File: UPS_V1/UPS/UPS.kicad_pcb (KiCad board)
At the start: 2 copper layers, 48.7 x 54.1 mm, 84 parts, among them J1 Conn_01x02_Pin, J2 Conn_01x02_Pin, J3 USB_B_Micro, J4 Conn_01x02_Socket, J5 Conn_01x02_Pin, J6 Conn_01x02_Socket, J7 Conn_01x02_Pin, J8 Screw_Terminal_01x02, J9 Screw_Terminal_01x02, U1 MT3608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

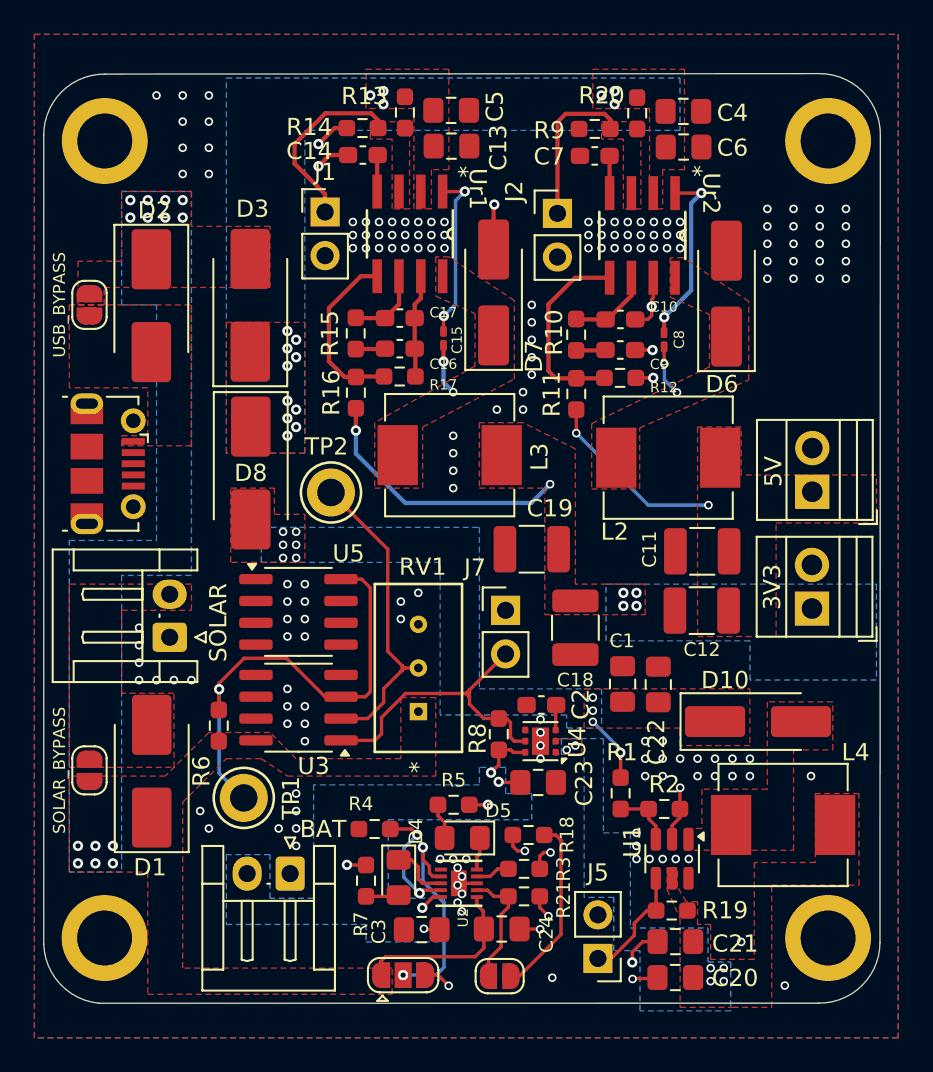
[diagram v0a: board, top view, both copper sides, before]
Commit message: added 1x12 terminal block
 1x12 terminal block
3d
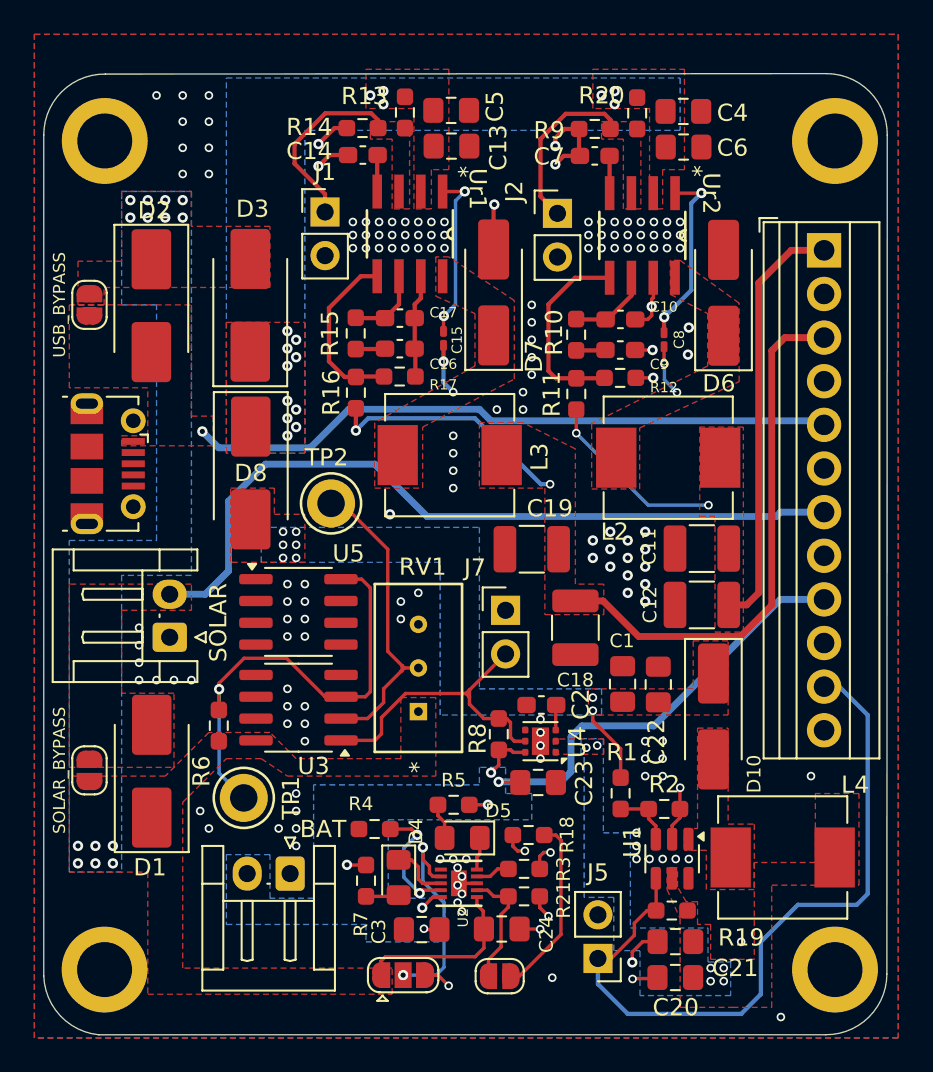
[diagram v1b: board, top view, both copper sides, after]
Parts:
- removed J9: Screw_Terminal_01x02, TerminalBlock:TerminalBlock_Xinya_XY308-2.54-2P_1x02_P2.54mm_Horizontal
- J8: value Screw_Terminal_01x02 -> PROVISIONAL_PORTS; footprint TerminalBlock:TerminalBlock_Xinya_XY308-2.54-2P_1x02_P2.54mm_Horizontal -> TerminalBlock:TerminalBlock_Xinya_XY308-2.54-12P_1x12_P2.54mm_Horizontal
- moved J8 20.9 mm to (159.8, 44.6), turned to -90 degrees
- moved D10 2.62 mm to (153.3, 71.7), turned to -90 degrees
- moved L4 1.89 mm to (157.4, 79.9)
- moved H2 1.88 mm to (160.4, 86.4)
- moved H1 1.84 mm to (117.9, 86.4)
- moved TP2 0.64 mm to (131.1, 59.3)
- moved H3 0.40 mm to (160.4, 38.2)
- moved C12 0.33 mm to (152.7, 65.2)
- moved D6 0.18 mm to (153.9, 47.0)
- moved C11 0.16 mm to (152.7, 61.9)
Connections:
- J5 pad 1: Net-(J5-Pin_1) -> BOOST_EN
- J8 pad 1: 3.3VOUT -> 5VOUT
- R19 pad 2: Net-(J5-Pin_1) -> BOOST_EN
- U1 pad 4: Net-(J5-Pin_1) -> BOOST_EN
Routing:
- net SOLAR IN: track 0.00 -> 45.0 mm
- net BOOST_EN: track 0.00 -> 43.1 mm
- net DC IN: track 0.00 -> 37.9 mm, vias 0 -> 1
- net 3.3VOUT: track 15.6 -> 45.7 mm, vias 6 -> 2
- net 5VOUT: track 10.8 -> 35.5 mm
- net BATT +: track 8.86 -> 33.4 mm
- net Net-(J5-Pin_1): track 6.84 -> 0.00 mm
- net GND: track 33.1 -> 38.4 mm, vias 173 -> 163
- net Net-(J2-Pin_1): track 9.27 -> 10.1 mm
- net Net-(D10-K): track 3.92 -> 4.57 mm, vias 10 -> 8
- removed copper zone on B.Cu, net 3.3VOUT
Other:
- board size 48.7 x 54.1 mm -> 49.1 x 56 mm
- board text added: "BATTERY"
- board text added: "BOOST_EN"
- board text added: "CTRL"
- board text added: "DC_IN"
- board text added: "DESIGN NOTES: VIAS SIZE: 0.6 & 0.3 0.5 & 0.3 TRACK SIZE USED: 0.4 0.2 0.25 COPPER ZONE FOR POWER: SOLID WITH 0.5 & 0.2 CLEARANCE COPPER ZONE FOR GND: THERMAL RELIEF 0.5 & 0.4 CLEARANCE *ADJUSTED CLEARANCE OF OTHER FOOTPRINT TOO BIG THAT CAUSES ERROR*"
- board text added: "GND"
- board text added: "INPUT"
- board text added: "OUTPUT"
- board text added: "SOLAR_IN"
- board text removed: "DESIGN NOTES: VIAS SIZE: 0.6 & 0.3 0.5 & 0.3 TRACK SIZE USED: 0.2 0.25 COPPER ZONE FOR POWER: SOLID WITH 0.5 & 0.2 CLEARANCE COPPER ZONE FOR GND: THERMAL RELIEF 0.5 & 0.4 CLEARANCE *ADJUSTED CLEARANCE OF OTHER FOOTPRINT TOO BIG THAT CAUSES ERROR*"

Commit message: minor edits
thermal reliefs
front silk designations
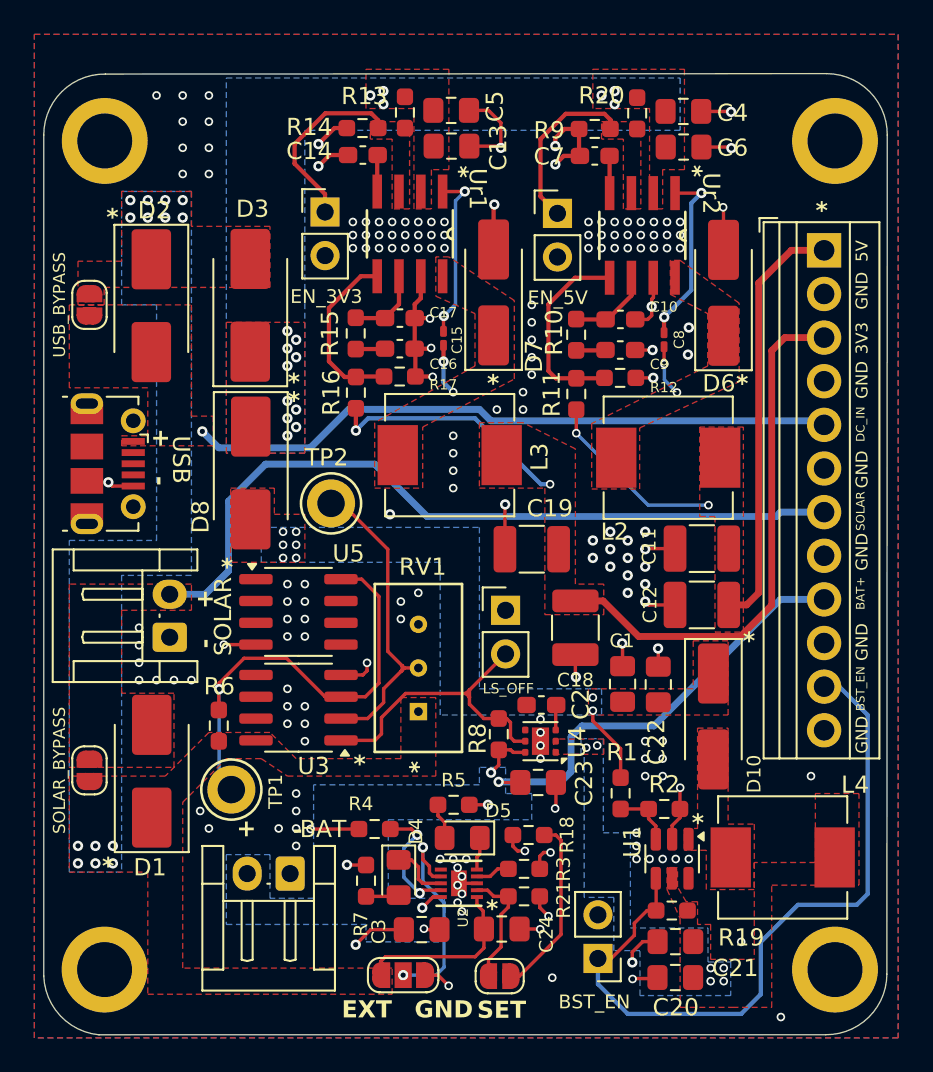
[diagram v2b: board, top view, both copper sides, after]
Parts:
- moved TP1 0.87 mm to (125.3, 76.0)
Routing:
- net GND: track 38.4 -> 75.7 mm, vias 163 -> 180
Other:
- board text added: "*"
- board text added: "BAT+"
- board text added: "BST_EN"
- board text added: "EXT"
- board text added: "SET"
- board text added: "SOLAR"

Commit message: -
edited zoning
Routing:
- net GND: vias 180 -> 259

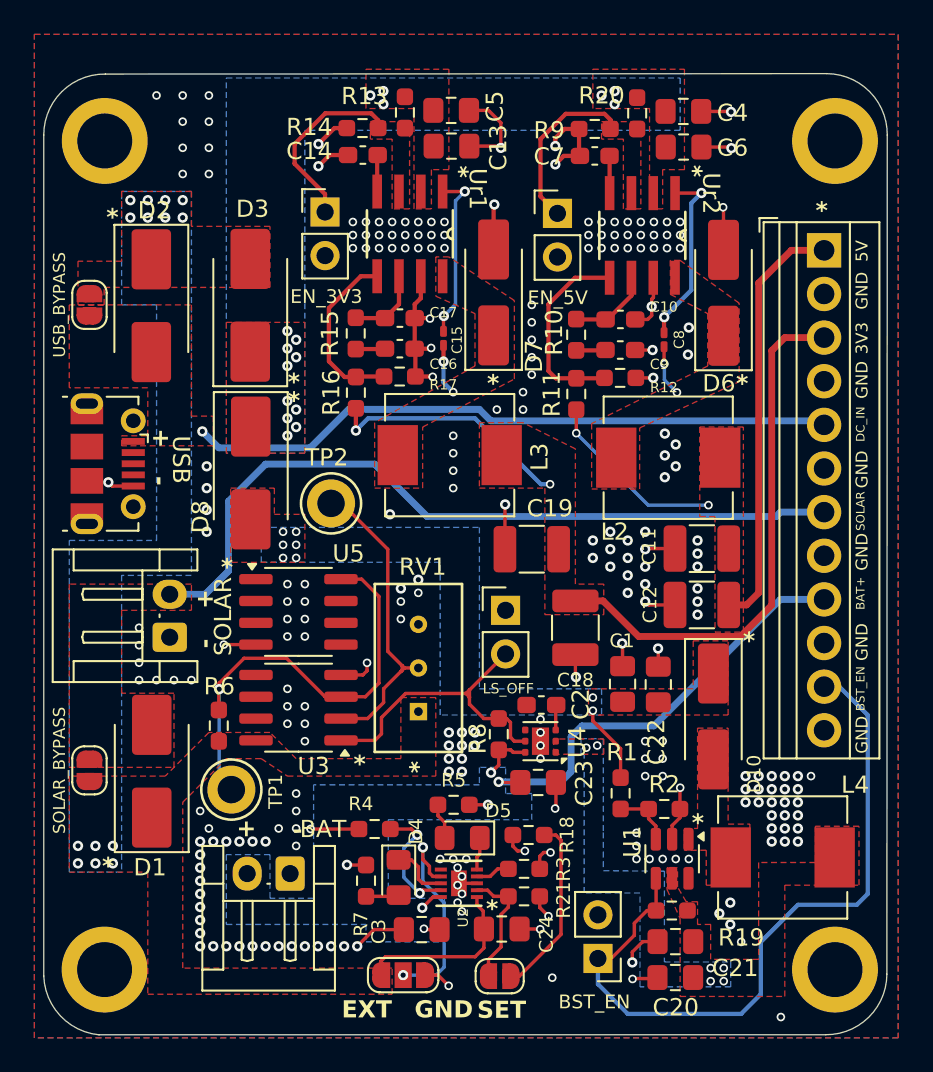
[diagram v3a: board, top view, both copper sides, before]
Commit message: Adjusted Silk Screen Front and Back
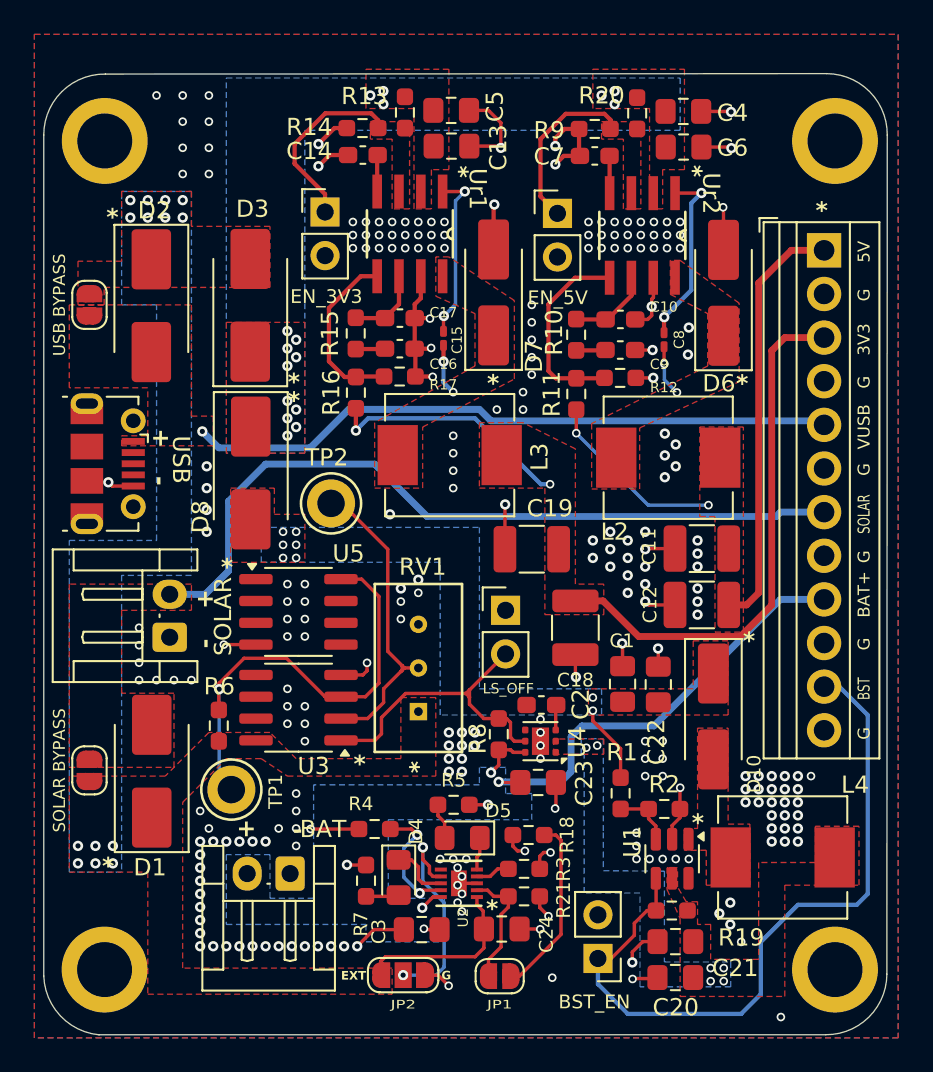
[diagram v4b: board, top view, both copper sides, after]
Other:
- board text added: "BST"
- board text added: "Charles Kim Kabiling Aernest Rivera"
- board text added: "Designed By:"
- board text added: "G"
- board text added: "INPUTS"
- board text added: "OUTPUTS"
- board text added: "VUSB"
- board text removed: "BST_EN"
- board text removed: "INPUT"
- board text removed: "OUTPUT"
- board text removed: "SET"
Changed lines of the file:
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@@
 			)
 		)
+		(model "${KICAD8_3DMODEL_DIR}/Potentiometer_THT.3dshapes/Potentiometer_Bourns_3266Y_Vertical.step"
+			(hide yes)
+			(offset
+				(xyz 5 0 0)
+			)
+			(scale
+				(xyz 1 1 1)
+			)
+			(rotate
+				(xyz 0 0 0)
+			)
+		)
+		(model "${KICAD8_3DMODEL_DIR}/Potentiometer_THT.3dshapes/Potentiometer_Bourns_3296W_Vertical.step"
+			(offset
+				(xyz 5 0 0)
+			)
+			(scale
+				(xyz 1 1 1)
+			)
+			(rotate
+				(xyz 0 0 0)
+			)
+		)
 	)
 	(footprint "Capacitor_SMD:C_0603_1608Metric_Pad1.08x0.95mm_HandSolder"
@@
 			(pintype "power_in")
 		)
-		(model "C:/Users/Aerest/Documents/GitHub/esp32PLC/UPS_V1/3D file/BQ24040DSQR/DSQ0010A.stp"
+		(model "C:/Users/ckabiling/OneDrive - Duke Manufacturing/Documents/Github/UPS/UPS_V1/3D file/BQ24040DSQR/DSQ0010A.stp"
 			(offset
 				(xyz 0 0 0)
@@
 			(pintype "power_in")
 		)
-		(model "C:/Users/Aerest/Documents/GitHub/esp32PLC/UPS_V1/3D file/TPS54331DR/D0008A.stp"
+		(model "C:/Users/ckabiling/OneDrive - Duke Manufacturing/Documents/Github/UPS/UPS_V1/3D file/TPS54331DR/D0008A.stp"
 			(offset
 				(xyz 0 0 0)
@@
 			)
 		)
-		(property "Designation" "USB_BYPASS"
+		(property "Designation" "USB BYPASS"
 			(at 0 1.75 90)
 			(unlocked yes)
@@
 		)
 		(model "C:/Users/Aerest/Documents/GitHub/esp32PLC/UPS_V1/3D file/1_282834_2/c-1-282834-2-c-3d.stp"
+			(hide yes)
 			(offset
 				(xyz 14 3.25 3)
@@
 			)
 			(rotate
-				(xyz -90 0 -180)
+				(xyz 0 0 -180)
+			)
+		)
+		(model "${KICAD8_3DMODEL_DIR}/TerminalBlock_Phoenix.3dshapes/TerminalBlock_Phoenix_MPT-0,5-6-2.54_1x06_P2.54mm_Horizontal.step"
+			(offset
+				(xyz 12.5 0 0)
+			)
+			(scale
+				(xyz 1 1 1)
+			)
+			(rotate
+				(xyz 0 0 180)
+			)
+		)
+		(model "${KICAD8_3DMODEL_DIR}/TerminalBlock_Phoenix.3dshapes/TerminalBlock_Phoenix_MPT-0,5-6-2.54_1x06_P2.54mm_Horizontal.step"
+			(offset
+				(xyz 28 0 0)
+			)
+			(scale
+				(xyz 1 1 1)
+			)
+			(rotate
+				(xyz 0 0 -180)
 			)
 		)
@@
 		(tags "solder jumper open")
 		(property "Reference" "JP2"
-			(at 0 -1.8 0)
+			(at 0.01 1.71 0)
 			(layer "F.SilkS")
-			(hide yes)
 			(effects
 				(font
-					(size 1 1)
-					(thickness 0.15)
+					(size 0.5 0.7)
+					(thickness 0.125)
 				)
 			)
@@
 			(pintype "power_in")
 		)
-		(model "C:/Users/Aerest/Documents/GitHub/esp32PLC/UPS_V1/3D file/TPS54331DR/D0008A.stp"
+		(model "C:/Users/ckabiling/OneDrive - Duke Manufacturing/Documents/Github/UPS/UPS_V1/3D file/TPS54331DR/D0008A.stp"
 			(offset
 				(xyz 0 0 0)
@@
 		(tags "solder jumper open")
 		(property "Reference" "JP1"
-			(at 0.135 -1.755002 0)
+			(at 0 1.65 0)
 			(layer "F.SilkS")
-			(hide yes)
 			(effects
 				(font
-					(size 1 1)
-					(thickness 0.15)
+					(size 0.5 0.7)
+					(thickness 0.125)
 				)
 			)
@@
 			)
 		)
-		(property "Designation" "SOLAR_BYPASS"
+		(property "Designation" "SOLAR BYPASS"
 			(at 0 -1.75 90)
 			(unlocked yes)
@@
 		(layer "Edge.Cuts")
 	)
-	(gr_text "OUTPUT"
+	(gr_text "OUTPUTS"
 		(at 162.73 47.66 90)
 		(layer "B.SilkS")
@@
 			(font
 				(size 1 1)
-				(thickness 0.1)
+				(thickness 0.15)
 			)
 			(justify left bottom mirror)
@@
 		)
 	)
-	(gr_text "INPUT"
+	(gr_text "INPUTS"
 		(at 162.6 61.6 90)
 		(layer "B.SilkS")
@@
 			(font
 				(size 1 1)
-				(thickness 0.1)
+				(thickness 0.15)
 			)
 			(justify left bottom mirror)
@@
 		)
 	)
+	(gr_text "Charles Kim Kabiling\nAernest Rivera"
+		(at 140.67 88.61 -0)
+		(layer "B.SilkS")
+		(effects
+			(font
+				(size 1 1.2)
+				(thickness 0.15)
+			)
+			(justify left bottom mirror)
+		)
+	)
 	(gr_text "GND"
 		(at 158.43 48.19 0)
@@
 	)
 	(gr_text "CTRL"
-		(at 161.4 73.24 -90)
+		(at 162.55 69.6 90)
+		(layer "B.SilkS")
+		(effects
+			(font
+				(size 1 1)
+				(thickness 0.15)
+			)
+			(justify left bottom mirror)
+		)
+	)
+	(gr_text "Designed By:\n"
+		(at 140.62 85.16 -0)
 		(layer "B.SilkS")
 		(effects
@@
 	)
 	(gr_text "SOLAR"
-		(at 162.18 60.91 90)
+		(at 162.5 61.083667 90)
 		(layer "F.SilkS")
 		(effects
 			(font
-				(size 0.5 0.5)
+				(size 0.7 0.5)
 				(thickness 0.1)
 			)
@@
 		)
 	)
-	(gr_text "GND"
-		(at 162.38 63.23 90)
+	(gr_text "G"
+		(at 162.5 62.787 90)
 		(layer "F.SilkS")
 		(effects
@@
 	)
 	(gr_text "BAT+"
-		(at 162.18 65.51 90)
+		(at 162.5 65.961286 90)
 		(layer "F.SilkS")
 		(effects
 			(font
-				(size 0.5 0.5)
+				(size 0.7 0.7)
 				(thickness 0.1)
 			)
@@
 		)
 	)
-	(gr_text "DC_IN"
-		(at 162.18 55.73 90)
+	(gr_text "VUSB"
+		(at 162.5 56.167 90)
 		(layer "F.SilkS")
 		(effects
 			(font
-				(size 0.5 0.5)
+				(size 0.7 0.7)
 				(thickness 0.1)
 			)
@@
 		)
 	)
-	(gr_text "GND"
-		(at 162.38 48.03 90)
+	(gr_text "G"
+		(at 162.5 47.547 90)
 		(layer "F.SilkS")
 		(effects
@@
 	)
 	(gr_text "5V"
-		(at 162.38 45.25 90)
+		(at 162.5 45.290334 90)
 		(layer "F.SilkS")
 		(effects
@@
 		)
 	)
-	(gr_text "GND"
-		(at 162.38 53.22 90)
+	(gr_text "G"
+		(at 162.5 52.627 90)
 		(layer "F.SilkS")
 		(effects
@@
 		)
 	)
-	(gr_text "GND"
-		(at 162.38 73.88 90)
+	(gr_text "G"
+		(at 162.5 73.07 90)
 		(layer "F.SilkS")
 		(effects
@@
 	)
 	(gr_text "3V3"
-		(at 162.38 50.63 90)
+		(at 162.5 50.703667 90)
 		(layer "F.SilkS")
 		(effects
@@
 	)
 	(gr_text "EXT"
-		(at 131.68 89.3545 0)
+		(at 131.64 87.09 0)
 		(layer "F.SilkS")
 		(effects
 			(font
-				(size 1 1)
-				(thickness 0.25)
+				(size 0.5 0.5)
+				(thickness 0.125)
 				(bold yes)
 			)
@@
 		)
 	)
-	(gr_text "BST_EN"
-		(at 162.18 71.4 90)
+	(gr_text "BST"
+		(at 162.5 70.755571 90)
 		(layer "F.SilkS")
 		(effects
 			(font
-				(size 0.5 0.5)
+				(size 0.7 0.5)
 				(thickness 0.1)
 			)
@@
 		)
 	)
-	(gr_text "GND"
-		(at 162.38 58.43 90)
+	(gr_text "G"
+		(at 162.5 57.707 90)
 		(layer "F.SilkS")
 		(effects
@@
 		)
 	)
-	(gr_text "SET"
-		(at 139.56 89.38 0)
-		(layer "F.SilkS")
-		(effects
-			(font
-				(size 1 1)
-				(thickness 0.2)
-				(bold yes)
-			)
-			(justify left bottom)
-		)
-	)
-	(gr_text "GND"
-		(at 135.92 89.3545 0)
+	(gr_text "G"
+		(at 137.49 87.08 0)
 		(layer "F.SilkS")
 		(effects
 			(font
-				(size 1 1)
-				(thickness 0.25)
+				(size 0.5 0.5)
+				(thickness 0.125)
 				(bold yes)
 			)
@@
 		)
 	)
-	(gr_text "GND"
-		(at 162.38 68.48 90)
+	(gr_text "G"
+		(at 162.5 67.867 90)
 		(layer "F.SilkS")
 		(effects

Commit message: -
updated symbol and footprint
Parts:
- C15, C8: footprint Capacitor_SMD:C_0201_0603Metric_Pad0.64x0.40mm_HandSolder -> Capacitor_SMD:C_0603_1608Metric_Pad1.08x0.95mm_HandSolder
- U4: value TPS22810DRV -> TPS22810DBVR; footprint Package_SON:WSON-6-1EP_2x2mm_P0.65mm_EP1x1.6mm -> InnovationCentral:SOT-23-6_L2.9-W1.6-P0.95-LS2.8-BL
- moved C23 1.25 mm to (142.9, 76.8)
- moved R8 1.05 mm to (139.8, 73.0)
- moved C8 0.70 mm to (151.1, 49.9)
- moved C15 0.41 mm to (137.9, 50.0)
- moved U4 0.35 mm to (143.3, 73.5), turned to -90 degrees
- moved C2 0.25 mm to (143.2, 70.8)
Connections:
- U4 pad 1: Net-(U1-IN) -> BATT +
- U4 pad 2: Net-(U1-IN) -> GND
- U4 pad 3: Net-(U4-CT) -> Net-(J7-Pin_2)
- U4 pad 4: GND -> Net-(U4-CT)
- U4 pad 5: Net-(J7-Pin_2) -> Net-(U1-IN)
- U4 pad 6: BATT + -> Net-(U1-IN)
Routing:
- net Net-(U4-CT): track 1.47 -> 7.00 mm, vias 0 -> 2
- net BATT +: track 33.4 -> 38.7 mm
- net Net-(J7-Pin_2): track 18.0 -> 20.9 mm, vias 0 -> 2
- net Net-(D6-K): track 2.97 -> 2.42 mm
- net GND: track 75.7 -> 75.6 mm, vias 259 -> 255
